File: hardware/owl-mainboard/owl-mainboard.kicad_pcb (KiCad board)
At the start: 4 copper layers, 61.8 x 79.8 mm, 107 parts, among them J101 Battery +, -, J201 USB-C, J202 EXP: GND, 3V3, A, B, J301 AMOLED FPC, J302 LRA, J303 DOCK: GND, VBUS, DET, GND, SW201 Ear left, SW202 Ear right, SW203 Beak, U101 BQ24073RGTR, U102 MAX17048G+T10, U103 TPS63802DLAR, U104 TPS22917DBVR, U201 ESP32-S3-WROOM-1-N16R8, U202 USBLC6-2SC6, U301 DRV2605LDGSR, U302 TMAG5273A2QDBVR, U303 LIS2DW12TR, U304 OPT3001DNPR, Y201 32.768kHz 12.5pF

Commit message: feat(hardware): label the power test pads on the back silkscreen
Review M6: bring-up probes TP101 (VIN_CHG), TP102 (VSYS), TP103 (VBAT)
and TP106 (GND) first, and their references are hidden. hw_silk.py now
writes VIN, VSYS and VBAT above the first three and GND below TP106,
0.8 mm high with the 0.15 mm stroke, each centred about 1.45 mm from
its own pad and nearer to it than to any other test pad, clear of pads,
holes, footprint silkscreen, the other marks, the boss keep-outs and
0.5 mm inside the edge. All four fit.

hw_place.py re-ran: R103's and R106's references give way to the VBAT
and VSYS labels, so 42 references are hidden now (was 40).
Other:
- board text added: "GND"
- board text added: "VBAT"
- board text added: "VIN"
- board text added: "VSYS"
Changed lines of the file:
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@@
 		(tags "resistor")
 		(property "Reference" "R106"
-			(at 1.58 0.92 0)
+			(at 0 0 90)
 			(layer "B.SilkS")
+			(hide yes)
 			(effects
 				(font
@@
 					(thickness 0.15)
 				)
-				(justify right mirror)
+				(justify mirror)
 			)
 		)
@@
 		(tags "resistor")
 		(property "Reference" "R103"
-			(at 1.58 -0.92 0)
+			(at 0 0 90)
 			(layer "B.SilkS")
+			(hide yes)
 			(effects
 				(font
@@
 					(thickness 0.15)
 				)
-				(justify left mirror)
+				(justify mirror)
 			)
 		)
@@
 		)
 	)
+	(gr_text "VBAT"
+		(locked yes)
+		(at 120.6 95.2 0)
+		(layer "B.SilkS")
+		(effects
+			(font
+				(size 0.8 0.8)
+				(thickness 0.15)
+			)
+			(justify mirror)
+		)
+	)
 	(gr_text "LRA"
 		(locked yes)
@@
 		)
 	)
+	(gr_text "VSYS"
+		(locked yes)
+		(at 128.9 95.6 0)
+		(layer "B.SilkS")
+		(effects
+			(font
+				(size 0.8 0.8)
+				(thickness 0.15)
+			)
+			(justify mirror)
+		)
+	)
+	(gr_text "VIN"
+		(locked yes)
+		(at 129.199999 104.1 0)
+		(layer "B.SilkS")
+		(effects
+			(font
+				(size 0.8 0.8)
+				(thickness 0.15)
+			)
+			(justify mirror)
+		)
+	)
+	(gr_text "GND"
+		(locked yes)
+		(at 129.199999 109.7 0)
+		(layer "B.SilkS")
+		(effects
+			(font
+				(size 0.8 0.8)
+				(thickness 0.15)
+			)
+			(justify mirror)
+		)
+	)
 	(gr_text "Tyukov Inc"
 		(locked yes)
@@
 	)
 	(group "hw_silk"
-		(members "28d5cabe-619d-446c-8603-362134bb7339" "3ce80490-8ddd-4d00-9fbe-55245bc62394"
-			"486126b5-384e-4703-90d4-6ca0bb9f1f16" "709f6162-fe5e-4085-91e6-eb69bc9a92ab"
-			"75c085e2-2d48-4509-ab3a-f99bfa317e4a" "77131891-ad04-41fb-a1a3-9e7400d74d69"
-			"783e5a4a-c5c7-440c-a29d-070fd06b84d0" "860d5eaf-0e2f-4ff7-8757-aa5427103a4e"
-			"adf8c87e-9cb2-42c6-beb5-8010df4854cf" "ae1d64db-30bf-4de2-a17a-ea3a9a00afe0"
-			"d1e42a76-bbcb-4f99-968e-ad059e4ceeb8" "e4eadd59-2e14-471f-ae39-6bfc3ffd6212"
-			"e8b0d548-e78a-4fe6-9c70-df295e29fe89" "ef0583d6-02fc-40c5-9a56-72759c95c33f"
-			"f26a8e6e-8b89-49cf-97cb-74ba5cfc6f58"
+		(members "09177cd9-b149-4248-8964-4bdff9a190cd" "139e736e-b77d-4eaf-ba97-787bf349b6fe"
+			"1dbb51b5-4826-4c76-a8ce-71e0d0a794d0" "1ff7ffd8-0e63-44ad-9fb8-3c439c6f0293"
+			"25f8de99-0087-4b09-8010-fa5480e198ef" "28b7aa73-80f1-4058-966b-4327b0292861"
+			"3b7d271c-1d3a-4581-a87d-ca1f1e1fa032" "52c506e2-3dd4-41cc-9bc6-01eebc2ad8e0"
+			"57867944-ed63-406e-95ef-8304141c17fe" "5f5b7efb-635f-4a62-bd0d-8d9d184d49df"
+			"63d178d1-38c9-4818-b35c-98a5d267ddde" "66320c09-deb2-4ab3-b9dd-83d2e38f3fa5"
+			"9158cdcc-a72d-444c-8f86-9d76ebba7fd8" "9d173d04-4b0b-4f1a-94a7-b78b58a2ec35"
+			"bf59e2e1-4289-4e9d-98a9-a1053f5520a1" "defc0365-e69b-415b-bff1-c5110bed39a1"
+			"f149b4ce-54fc-41b1-a3bb-1bff7f4877bf" "f502ee5a-2a0a-43f6-a702-ff931ebe48a2"
+			"f638aa78-56d8-4140-af79-86901c78ed67"
 		)
 	)

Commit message: fix(hardware): set the charge current to at most 0.5 C of the 700 mAh pack
Controller ruling: the BQ24073 fast-charge current may not exceed 0.5 C of the EEMB 700 mAh
fallback pack, 0.35 A. ICHG = KISET / RISET with KISET 797, 890, 975 A-ohm (SLUS810N p. 13);
with KISET at 975 and the resistor 1 % low, RISET must be at least 975 / 0.35 / 0.99 = 2.81k.
JLC lists 2.8k (C62741), 2.87k (C113479), 2.94k (C25886) and 3k (C25784) as Extended; the
nearest Basic value at or above is 3.3k, 0402WGF3301TCE (C25890, 1986011 in stock).

R101 2k (C4109) -> 3.3k (C25890): ICHG 0.270 A typical, 0.239 to 0.298 A (0.43 C of 700 mAh,
0.40 C of 740 mAh at worst); precharge 27 mA, termination about 27 mA. ICHG is now below the
input limit (0.369 to 0.478 A), so the cell charges at ICHG unless the system load takes the
input to its limit. U101's worst-case dissipation falls from about 0.77 W to 0.51 W.

design.toml, the schematic value and fields, the board (hw_sync), rev-a.md (calculations, the
smaller-cell note, the RT101 bring-up item, a decisions row), bringup.md step 9 and the review's
BQ24073 and thermal rows follow. hw_fab 0 errors (top 6, bottom 81; BOM row R101 3.3k C25890),
hw_stock 43 unique parts, 0 low; ERC 0, DRC 0/0/0 with parity, check_all 0, tools tests 110.
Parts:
- R101: value 2k -> 3.3k
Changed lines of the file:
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@@
 			)
 		)
-		(property "Value" "2k"
+		(property "Value" "3.3k"
 			(at 0 -1.17 180)
 			(layer "B.Fab")
@@
 			)
 		)
-		(property "LCSC Part #" "C4109"
+		(property "LCSC Part #" "C25890"
 			(at 0 0 180)
 			(layer "B.SilkS")
@@
 			)
 		)
-		(property "MPN" "0402WGF2001TCE"
+		(property "MPN" "0402WGF3301TCE"
 			(at 0 0 180)
 			(layer "B.SilkS")

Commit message: feat(hardware): place the touch level shift and the moved J301 on the main board
hw_sync.py brings U305, U306, C311, C312 and R310 to R315 onto the
board and moves J301 pins 27 to 30 to the TP_*_1V8 nets; R315 takes
DNP, exclude from BOM and exclude from position files from its symbol.
hw_contract.py apply moves and locks J301 at (-5.00, 4.22) rot 270 and
draws the new "display adapter path" keep-out.

hw_place.py: C301 and C302 at the section 2 points east of J301's
DISP_3V3 pins. The section 2 points for the translator overlapped
(U305's courtyard is 7.8 mm wide), so the block is laid out again
outside the actuator strip x -3.7 to -2.4: U305 at (2.0, -1.6); the
1.8 V pull-ups in a row below it at y -5.6, in pin order (RST, INT,
SCL, SDA from the west) so their tracks come down under the package
without crossing, R310 at the row's west end; C312 under pin 8 beside
U306 at (8.0, -4.85); R315 and C311 below U306. R301 to R303 move to
the front beside U305's B pins (design.toml side "front"), which frees
the back between the module and J301 for the QSPI lanes. No new pad
covers a via without tracks: on save pcbnew gives such a via the net
of the pad over it.

hw_silk.py: J301's "1" and "31" marks at (-5.0, 10.7) and (-5.0, -2.3).
The PCB title block and the back silkscreen date move to 2026-10-13.
hw_contract.py apply redraws Edge.Cuts, so the three silk_edge
exclusions are rekeyed to the new edge segments, comments unchanged.

Routing comes next: DRC has 66 violations, all routing (no courtyard
overlap), 49 unconnected items and 0 parity. ERC 0, contract 0 errors,
title blocks 0 errors, fit check 0 clashes, enclosure suite 139 passed.
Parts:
- added C311: 1uF, Capacitor_SMD:C_0402_1005Metric, F.Cu at (109.4, 107.2)
- added C312: 1uF, Capacitor_SMD:C_0402_1005Metric, F.Cu at (105.2, 105.4)
- added R310: 100k, Resistor_SMD:R_0402_1005Metric, F.Cu at (98.1, 105.4)
- added R311: 4.7k, Resistor_SMD:R_0402_1005Metric, F.Cu at (103.2, 105.6)
- added R312: 4.7k, Resistor_SMD:R_0402_1005Metric, F.Cu at (101.7, 105.6)
- added R313: 10k, Resistor_SMD:R_0402_1005Metric, F.Cu at (100.5, 105.6)
- added R314: 10k, Resistor_SMD:R_0402_1005Metric, F.Cu at (99.3, 105.6)
- added R315: 0R, Resistor_SMD:R_0402_1005Metric, F.Cu at (107.4, 107.3)
- added U305: LSF0204PWR, Package_SO:TSSOP-14_4.4x5mm_P0.65mm, F.Cu at (102.0, 101.6)
- added U306: XC6206P182MR, Package_TO_SOT_SMD:SOT-23-3, F.Cu at (108.0, 104.8)
- R301, R302, R303: moved to F.Cu
- moved R303 21.1 mm to (107.9, 102.5), turned to 180 degrees
- moved R302 19.1 mm to (107.9, 101.0), turned to 180 degrees
- moved R301 17.2 mm to (107.9, 99.3), turned to 180 degrees
- moved J301 9.25 mm to (95.0, 95.8), turned to -90 degrees
- moved C302 7.28 mm to (98.8, 98.1)
- moved C301 5.11 mm to (98.8, 97.0)
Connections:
- J301 pad 27: TP_SCL -> TP_SCL_1V8
- J301 pad 28: TP_SDA -> TP_SDA_1V8
- J301 pad 29: TP_RST -> TP_RST_1V8
- J301 pad 30: TP_INT -> TP_INT_1V8
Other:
- board text added: "2026-10-13"
- board text removed: "2026-10-11"

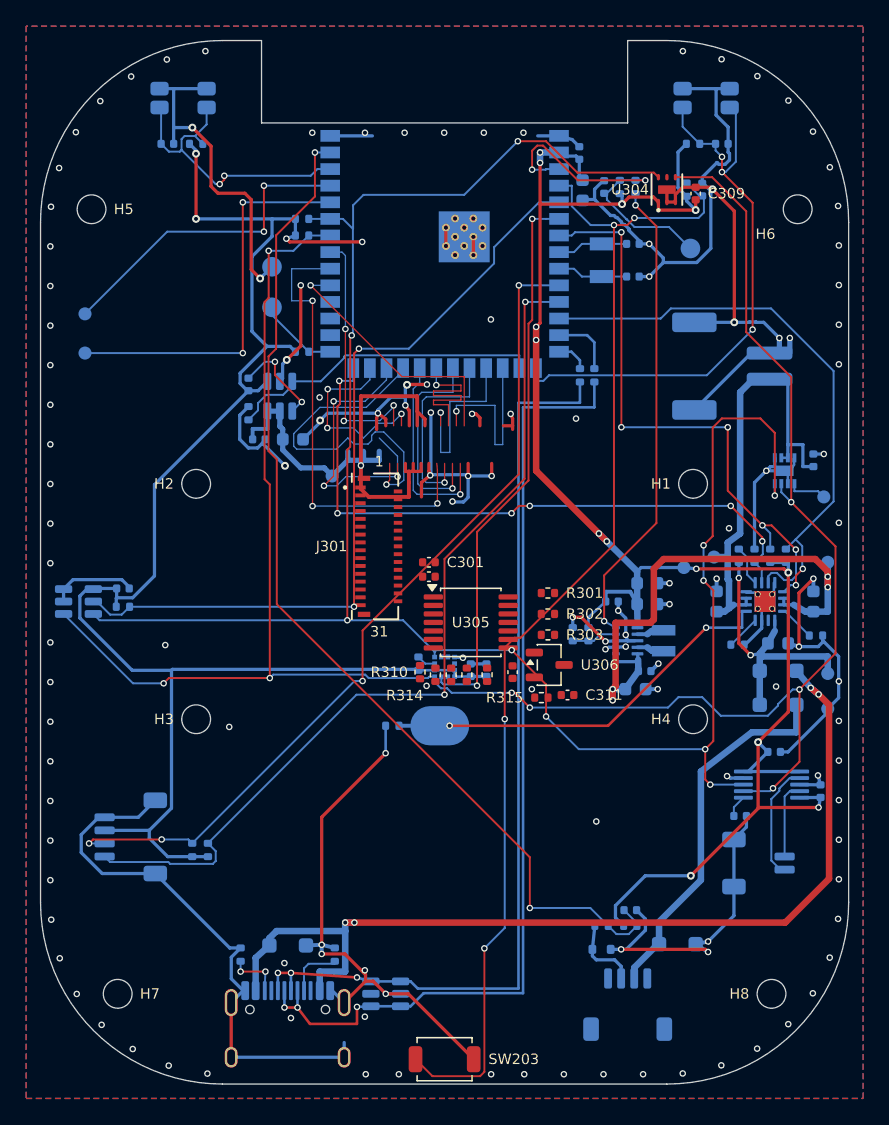
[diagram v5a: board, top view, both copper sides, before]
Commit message: feat(hardware): hand-route J301's new position and the touch level shift
Delete the copper the moved J301 and the new translator block sit on: every
Freerouting track and via of TP_SDA, TP_SCL, TP_INT and TP_RST; the F.Cu
segments of EXP_A, EXP_B, HALL_INT, I2C_SDA, IMU_INT1 and BTN_BEAK that touch
x -9 to 9, y -9 to 11, with the vias I2C_SDA (5.13, -3.72) and (-7.44, -1.43)
and HALL_INT (-6.93, -0.40); CHG_SUSPEND's copper in that window (it ran under
J301's new position); the GND links to the old qspi and j301_fanout vias; and
the stubs this leaves dangling (KiCad's own dangling test).

hw_route.py: j301_comb() for J301 at rotation 270 (rows along y), new qspi,
j301_fanout and disp_3v3 groups, and a new touch_shift group for U305, U306,
the 1.8 V and 3.3 V pull-ups and the ESP32-S3 side of the touch lines. QSPI
lengths 19.5 to 26.5 mm, LCD_CLK 23.2 mm. The remaining displaced nets go to
Freerouting next.
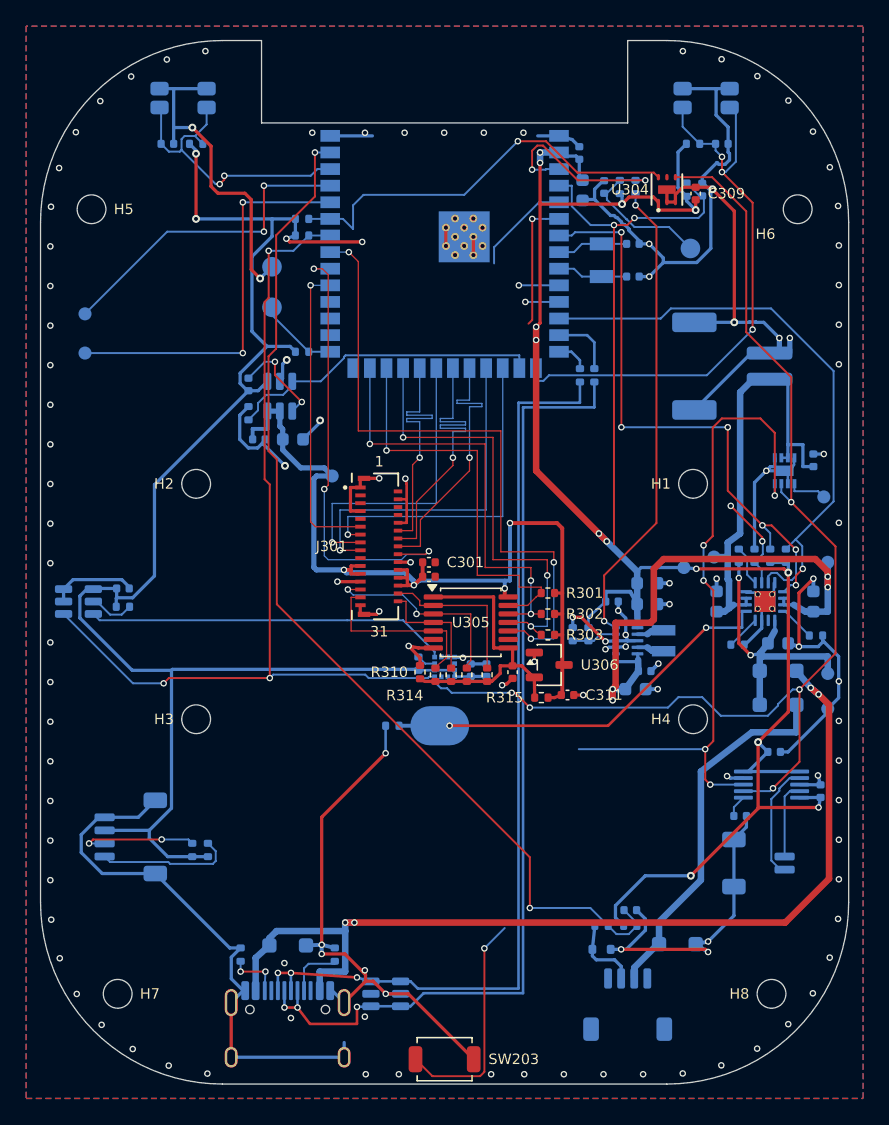
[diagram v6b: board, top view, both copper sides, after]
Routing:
- net EXP_B: track 68.4 -> 13.1 mm, vias 2 -> 1
- net EXP_A: track 65.8 -> 12.4 mm, vias 4 -> 3
- net HALL_INT: track 61.2 -> 11.1 mm, vias 2 -> 0
- net I2C_SDA: track 157.2 -> 111.4 mm, vias 10 -> 6
- net CHG_SUSPEND: track 50.0 -> 7.38 mm, vias 6 -> 2
- net BTN_BEAK: track 91.7 -> 58.6 mm, vias 4 -> 3
- net IMU_INT1: track 42.7 -> 10.2 mm, vias 2 -> 1
- net TP_RST: track 19.9 -> 49.5 mm
- net DISP_3V3: track 42.4 -> 69.0 mm, vias 1 -> 4
- net DISP_1V8: track 0.00 -> 21.8 mm
- net GND: track 346.4 -> 325.0 mm, vias 130 -> 117
- net TP_SCL: track 15.0 -> 33.1 mm
- net TP_SCL_1V8: track 0.00 -> 14.8 mm, vias 0 -> 2
- net TP_RST_1V8: track 0.00 -> 12.9 mm
- net LCD_CS: track 14.0 -> 26.5 mm
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
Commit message: feat(hardware): route the nets the moved J301 displaced
Freerouting 2.4.1 (only these nets connectable in the DSN, every other track
and via fixed, In1 and In2 as power layers without planes) routed HALL_INT,
CHG_SUSPEND, BTN_BEAK and the I2C_SDA link from U303 to the U301 side; the
session's wires for those nets were added to the board, nothing else. It left
EXP_A, EXP_B, IMU_INT1 and the I2C_SDA link from U304 unrouted after two runs:
EXP_A and EXP_B (3 vias each, round the west edge to J202) and the U304 link
(east of TPS_PG to U102's run) come from a grid router with the same class
clearances, kept off the antenna end, the crystal, U302 and L101.

hw_route.py: late_links gains IMU_INT1 (U303 pin 12 up a B.Cu lane beside the
USB pair to its run from module pin 6, one via); touch_shift moves its
DISP_3V3 crossing to x 4.75 and the four touch lanes 0.1 mm west to make room.
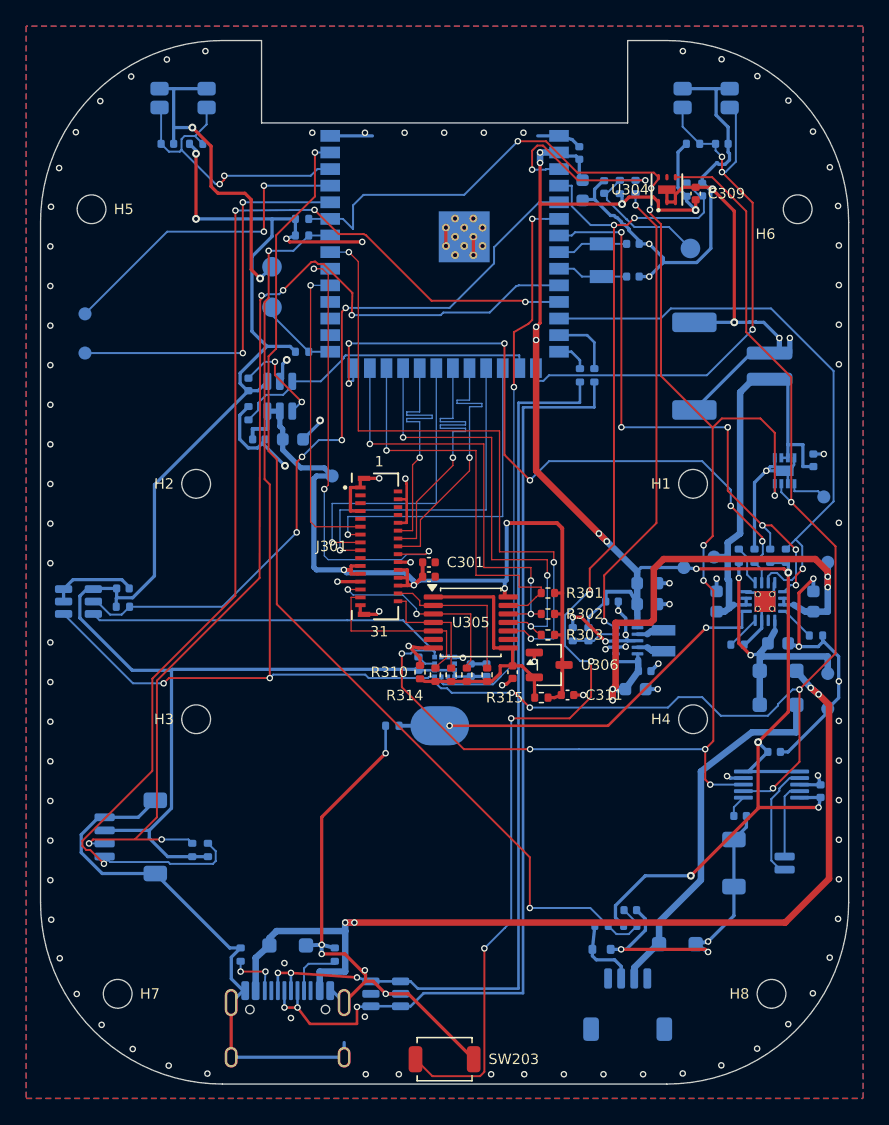
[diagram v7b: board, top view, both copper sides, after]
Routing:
- net EXP_B: track 13.1 -> 93.9 mm, vias 1 -> 4
- net EXP_A: track 12.4 -> 82.3 mm, vias 3 -> 5
- net HALL_INT: track 11.1 -> 58.7 mm, vias 0 -> 4
- net CHG_SUSPEND: track 7.38 -> 53.1 mm, vias 2 -> 6
- net I2C_SDA: track 111.4 -> 153.2 mm, vias 6 -> 10
- net BTN_BEAK: track 58.6 -> 96.3 mm, vias 3 -> 6
- net IMU_INT1: track 10.2 -> 43.5 mm, vias 1 -> 2
